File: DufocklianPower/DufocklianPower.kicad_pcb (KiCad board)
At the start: 0 parts

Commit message: finish pcb
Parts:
- added C1: 100n, Capacitor_SMD:C_0805_2012Metric, F.Cu at (175.1, 88.9)
- added C10: 4.7u, Capacitor_SMD:C_0805_2012Metric, F.Cu at (190.6, 72.9)
- added C11: 10u, Capacitor_SMD:C_0805_2012Metric, F.Cu at (190.6, 76.9)
- added C15: 100n, Capacitor_SMD:C_1210_3225Metric, F.Cu at (138.2, 89.6)
- added C16: 100n, Capacitor_SMD:C_1210_3225Metric, F.Cu at (147.9, 101.4)
- added C17: 100n, Capacitor_SMD:C_1210_3225Metric, F.Cu at (142.9, 89.6)
- added C18: 100n, Capacitor_SMD:C_1210_3225Metric, F.Cu at (147.9, 96.7)
- added C19: 100n, Capacitor_SMD:C_0805_2012Metric, F.Cu at (162.8, 80.3)
- added C2: 1u, Capacitor_SMD:C_0805_2012Metric, F.Cu at (146.6, 57.7)
- added C20: 1u, Capacitor_SMD:C_0805_2012Metric, F.Cu at (160.7, 80.3)
- added C21: 22u, Capacitor_SMD:C_1210_3225Metric, F.Cu at (176.8, 99.9)
- added C22: 22u, Capacitor_SMD:C_1210_3225Metric, F.Cu at (173.6, 95.3)
- added C23: 22u, Capacitor_SMD:C_1210_3225Metric, F.Cu at (176.8, 95.3)
- added C24: 22u, Capacitor_SMD:C_1210_3225Metric, F.Cu at (173.6, 99.9)
- added C25: 100n, Capacitor_SMD:C_0805_2012Metric, F.Cu at (166.2, 91.8)
- added C26: 1u, Capacitor_SMD:C_0805_2012Metric, F.Cu at (153.4, 78.8)
- added C27: 47u, Capacitor_SMD:C_0805_2012Metric, F.Cu at (158.3, 72.3)
- added C3: 1u, Capacitor_SMD:C_0805_2012Metric, F.Cu at (146.6, 51.3)
- added C36: 100p, Capacitor_SMD:C_0805_2012Metric, F.Cu at (175.1, 85.4)
- added C37: 100n, Capacitor_SMD:C_0805_2012Metric, F.Cu at (151.1, 57.3)
- added C38: 100n, Capacitor_SMD:C_0805_2012Metric, F.Cu at (183.2, 69.8)
- added C4: 1u, Capacitor_SMD:C_0805_2012Metric, F.Cu at (193.8, 104.1)
- added C40: 100n, Capacitor_SMD:C_0805_2012Metric, F.Cu at (193.8, 100.7)
- added C42: 100p, Capacitor_SMD:C_0805_2012Metric, F.Cu at (182.7, 78.5)
- added C43: 1n, Capacitor_SMD:C_0805_2012Metric, F.Cu at (184.7, 78.5)
- added C44: 2.2n, Capacitor_SMD:C_0805_2012Metric, F.Cu at (180.9, 75.0)
- added C6: 2.2n, Capacitor_SMD:C_0805_2012Metric, F.Cu at (193.0, 54.1)
- added C7: 56p, Capacitor_SMD:C_0805_2012Metric, F.Cu at (193.0, 56.1)
- added C8: 2.2n, Capacitor_SMD:C_0805_2012Metric, F.Cu at (188.4, 53.0)
- added C9: 1u, Capacitor_SMD:C_0805_2012Metric, F.Cu at (190.6, 74.9)
- added J1: 8174, Library:KEYSTONE_8174, F.Cu at (140.5, 99.0)
- added J2: SCREEN, Connector_PinHeader_2.54mm:PinHeader_1x04_P2.54mm_Vertical, F.Cu at (213.5, 101.8)
- added J3: 8174, Library:KEYSTONE_8174, F.Cu at (140.5, 80.0)
- added J4: USB_C_Receptacle_USB2.0_14P, Connector_USB:USB_C_Receptacle_GCT_USB4105-xx-A_16P_TopMnt_Horizontal, F.Cu at (139.2, 65.2)
- added J5: OUT, Connector_AMASS:AMASS_XT60PW-M_1x02_P7.20mm_Horizontal, F.Cu at (190.8, 110.9)
- added L1: 15uH, Library:IND_SER2915H-223KL, F.Cu at (159.6, 115.1)
- added L2: 68uH, Library:IND_BOURNS_SRR1260, F.Cu at (202.4, 59.5)
- added Q1: NMOS, Library:TRANS_BSC027N10NS5ATMA1, F.Cu at (161.3, 94.7)
- added Q2: NMOS, Library:TRANS_BSC027N10NS5ATMA1, F.Cu at (160.7, 88.1)
- added Q4: 2N7002, Package_TO_SOT_SMD:SOT-23, F.Cu at (179.0, 89.8)
- added R1: 87k, Resistor_SMD:R_0603_1608Metric, F.Cu at (169.2, 80.5)
- added R10: 14k7, Resistor_SMD:R_0603_1608Metric, F.Cu at (166.1, 80.5)
- added R11: 400k, Resistor_SMD:R_0603_1608Metric, F.Cu at (194.9, 80.1)
- added R12: 100k, Resistor_SMD:R_0603_1608Metric, F.Cu at (158.9, 80.3)
- added R13: 100k, Resistor_SMD:R_0603_1608Metric, F.Cu at (170.7, 80.5)
- added R14: 100k, Resistor_SMD:R_0603_1608Metric, F.Cu at (196.4, 80.1)
- added R16: 1k, Resistor_SMD:R_0603_1608Metric, F.Cu at (180.9, 78.3)
- added R17: 10k, Resistor_SMD:R_0603_1608Metric, F.Cu at (151.0, 53.9)
- added R19: 10k, Resistor_SMD:R_0603_1608Metric, F.Cu at (183.4, 76.0)
- added R2: 10.7k, Resistor_SMD:R_0603_1608Metric, F.Cu at (175.1, 87.2)
- added R20: 4.7k, Resistor_SMD:R_0603_1608Metric, F.Cu at (175.1, 90.7)
- added R21: 120k, Resistor_SMD:R_0603_1608Metric, F.Cu at (154.0, 73.1)
- added R22: 5m, Resistor_SMD:R_0603_1608Metric, F.Cu at (158.3, 75.5)
- added R23: 2m, Library:FC4L90_OHM, F.Cu at (184.8, 95.3)
- added R24: 1k, Resistor_SMD:R_0603_1608Metric, F.Cu at (179.0, 85.5)
- added R25: 10k, Resistor_SMD:R_0603_1608Metric, F.Cu at (181.5, 69.8)
- added R26: 2.7k, Resistor_SMD:R_0603_1608Metric, F.Cu at (155.6, 60.2)
- added R27: 2.7k, Resistor_SMD:R_0603_1608Metric, F.Cu at (155.6, 61.7)
- added R28: 2m, Library:FC4L90_OHM, F.Cu at (185.5, 104.2)
- added R29: 2.7k, Resistor_SMD:R_0603_1608Metric, F.Cu at (211.5, 67.9)
- added R3: 100k, Resistor_SMD:R_0603_1608Metric, F.Cu at (190.8, 62.9)
- added R30: 5.1k, Resistor_SMD:R_0603_1608Metric, F.Cu at (146.1, 67.0)
- added R31: 5.1k, Resistor_SMD:R_0603_1608Metric, F.Cu at (146.6, 63.0)
- added R32: 100k, Resistor_SMD:R_0603_1608Metric, F.Cu at (179.0, 87.1)
- added R33: 100, Resistor_SMD:R_0603_1608Metric, F.Cu at (194.0, 105.9)
- added R34: 100, Resistor_SMD:R_0603_1608Metric, F.Cu at (193.8, 102.4)
- added R35: 2.7k, Resistor_SMD:R_0603_1608Metric, F.Cu at (206.4, 122.5)
- added R4: 316k, Resistor_SMD:R_0603_1608Metric, F.Cu at (193.0, 57.9)
- added R5: 101k, Resistor_SMD:R_0603_1608Metric, F.Cu at (193.0, 59.3)
- added R6: 470k, Resistor_SMD:R_0603_1608Metric, F.Cu at (193.0, 52.4)
- added R7: 5m, Resistor_SMD:R_2512_6332Metric, F.Cu at (154.3, 93.5)
- added R8: 615k, Resistor_SMD:R_0603_1608Metric, F.Cu at (164.6, 80.5)
- added R9: 10k, Resistor_SMD:R_0603_1608Metric, F.Cu at (167.6, 80.5)
- added SW1: RST, Button_Switch_SMD:SW_Push_1P1T-SH_NO_CK_KMR2xxG, F.Cu at (154.2, 55.0)
- added SW2: BOOT, Button_Switch_SMD:SW_Push_1P1T-SH_NO_CK_KMR2xxG, F.Cu at (178.9, 68.7)
- added SW3: Voltage Control, Rotary_Encoder:RotaryEncoder_Alps_EC11E-Switch_Vertical_H20mm, F.Cu at (205.7, 84.8)
- added SW4: Current Control, Rotary_Encoder:RotaryEncoder_Alps_EC11E-Switch_Vertical_H20mm, F.Cu at (210.6, 105.5)
- added U1: ~, Library:VQFN24_RGY_TEX, F.Cu at (168.3, 86.7)
- added U11: INA228, Package_SO:TSSOP-10_3x3mm_P0.5mm, F.Cu at (193.6, 95.6)
- added U2: LM5164DDA, Package_SO:HSOP-8-1EP_3.9x4.9mm_P1.27mm_EP2.41x3.1mm_ThermalVias, F.Cu at (186.7, 60.5)
- added U3: ADS8681RUM, Package_DFN_QFN:QFN-16-1EP_4x4mm_P0.65mm_EP2.7x2.7mm, F.Cu at (196.6, 74.6)
- added U4: DAC8562, Package_SO:TSSOP-10_3x3mm_P0.5mm, F.Cu at (165.0, 76.3)
- added U5: INA241A4xD, Package_SO:SOIC-8_3.9x4.9mm_P1.27mm, F.Cu at (184.9, 85.6)
- added U6: ESP32-S3-WROOM-1, RF_Module:ESP32-S3-WROOM-1, F.Cu at (167.2, 54.1)
- added U7: OPA188xxD, Package_SO:SOIC-8_3.9x4.9mm_P1.27mm, F.Cu at (176.2, 78.4)
- added U8: AP2112K-3.3, Package_TO_SOT_SMD:SOT-23-5, F.Cu at (146.6, 54.5)
- added U9: REF6025xDGK, Package_SO:VSSOP-8_3x3mm_P0.65mm, F.Cu at (153.5, 75.9)
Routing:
- net +3V3: track 0.00 -> 217.1 mm, vias 0 -> 8
- net VBUS: track 0.00 -> 83.6 mm, vias 0 -> 59
- net /C_{CF}: track 0.00 -> 79.0 mm
- net /SCL: track 0.00 -> 76.4 mm, vias 0 -> 2
- net /SDA: track 0.00 -> 75.7 mm, vias 0 -> 2
- net /CEN_{B}: track 0.00 -> 72.2 mm
- net /CEN_{A}: track 0.00 -> 70.0 mm
- net /VOUT_{0}: track 0.00 -> 56.0 mm, vias 0 -> 46
- net /~{RST}: track 0.00 -> 55.1 mm
- net +5V: track 0.00 -> 53.4 mm, vias 0 -> 5
- net /SDI: track 0.00 -> 52.0 mm
- net /VEN_{B}: track 0.00 -> 50.3 mm
- net /~{ALRT}: track 0.00 -> 49.9 mm, vias 0 -> 2
- net /VEN_{A}: track 0.00 -> 46.5 mm
- net /~{CS}: track 0.00 -> 42.4 mm
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- added copper zone on In2.Cu, net +5V
- added copper zone on F.Cu, net /ISNS+
- added copper zone on F.Cu, net /SW
- added copper zone on F.Cu, net /VOUT
- added copper zone on F.Cu, net /VOUT_{0}
- added copper zone on In2.Cu, net /VOUT_{0}
- added copper zone on F.Cu, net /VOUT_{1}
- added copper zone on B.Cu, net GNDREF
- added copper zone on F.Cu, net GNDREF
- added copper zone on In1.Cu, net GNDREF
- added copper zone on F.Cu, net VBUS
- added copper zone on In2.Cu, net VBUS
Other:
- board outline added: 80 x 80 mm
- copper layers 0 -> 4
- board text added: "{ "ViaStitcher": "0.3.4", "stitch_zone_0": { "HSpacing": "1", "VSpacing": "1", "HOffset": "0", "VOffset": "0", "Clearance": "0", "FillStyle": "Standard", "OnlyFilledCopper": true } }"
- board text added: "{ "ViaStitcher": "0.3.4", "stitch_zone_0": { "HSpacing": "5", "VSpacing": "5", "HOffset": "0", "VOffset": "0", "Clearance": "0", "FillStyle": "Stagger", "OnlyFilledCopper": true } }"

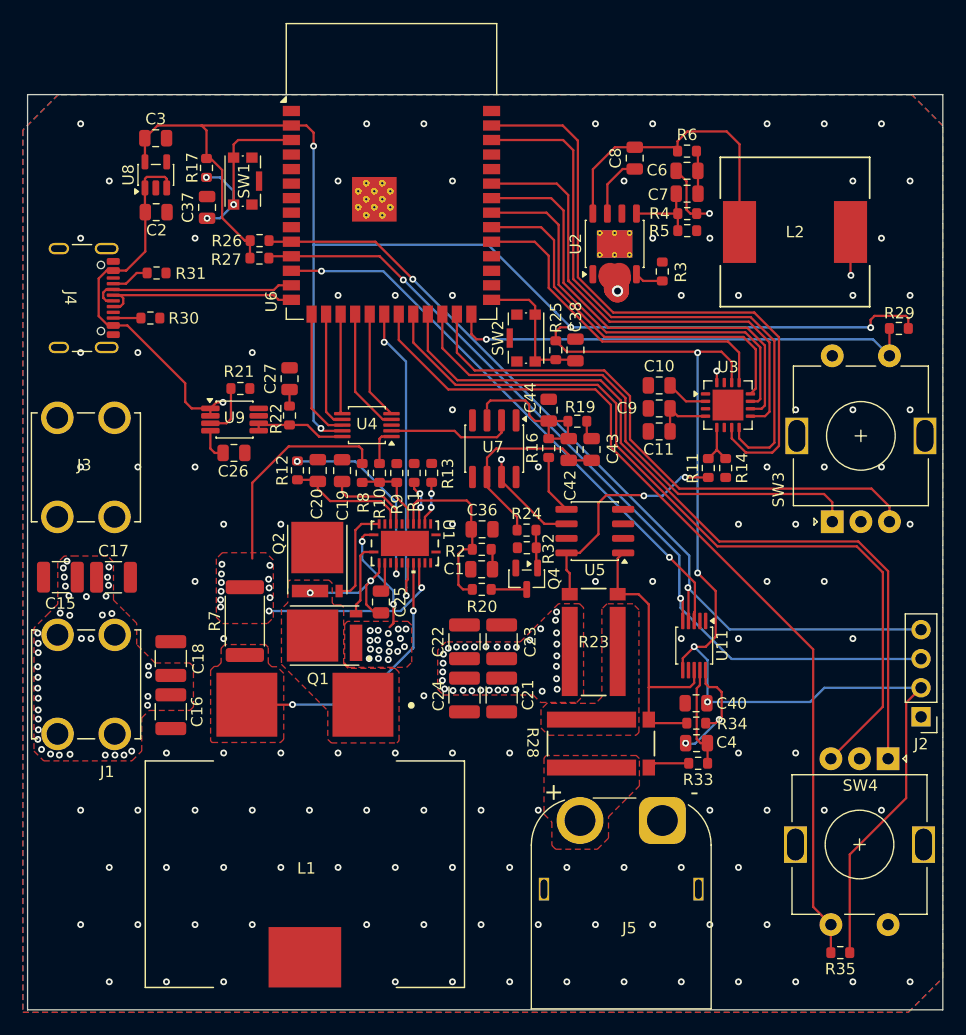
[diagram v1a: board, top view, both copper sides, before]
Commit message: finish via + change ind
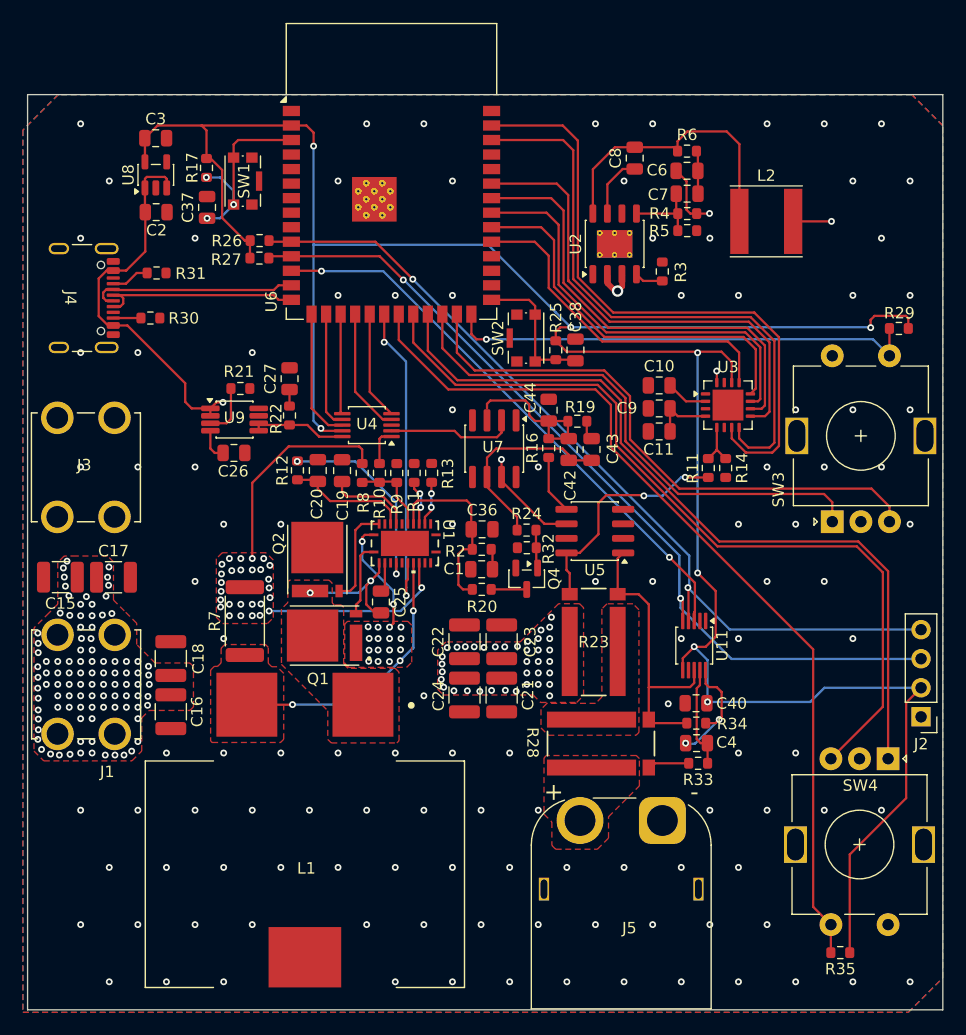
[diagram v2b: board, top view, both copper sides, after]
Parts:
- L2: footprint Library:IND_BOURNS_SRR1260 -> Inductor_SMD:L_Taiyo-Yuden_NR-60xx
- moved L2 2.68 mm to (199.9, 58.5)
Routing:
- net VBUS: track 83.6 -> 83.1 mm, vias 59 -> 117
- net GNDREF: vias 115 -> 116
- net /VOUT_{0}: vias 46 -> 68
- net /ISNS+: vias 2 -> 3

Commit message: less drc
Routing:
- net GNDREF: vias 116 -> 118
- net /ISNS+: vias 3 -> 2
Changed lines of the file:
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@@
 	)
 	(via
+		(at 179.61 62.63)
+		(size 0.6)
+		(drill 0.3)
+		(layers "F.Cu" "B.Cu")
+		(free yes)
+		(net "GNDREF")
+	)
+	(via
 		(at 172.5 105)
 		(size 0.6)
@@
 	)
 	(via
+		(at 176.49 67.69)
+		(size 0.6)
+		(drill 0.3)
+		(layers "F.Cu" "B.Cu")
+		(free yes)
+		(net "GNDREF")
+	)
+	(via
 		(at 210 80)
 		(size 0.6)
@@
 	)
 	(via
-		(at 167.925 96.935)
-		(size 0.6)
-		(drill 0.3)
-		(layers "F.Cu" "B.Cu")
-		(net "/ISNS+")
-	)
-	(via
 		(at 158.52 100.77)
 		(size 0.6)
@@
 			(smoothing fillet)
 			(radius 0.2)
-			(island_removal_mode 1)
+			(island_removal_mode 2)
+			(island_area_min 25)
 		)
 		(polygon

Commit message: bom.csv
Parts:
- removed C21, C23, C24: 22u, Capacitor_SMD:C_1210_3225Metric
- removed J5: OUT, Connector_AMASS:AMASS_XT60PW-M_1x02_P7.20mm_Horizontal
- removed U7: OPA188xxD, Package_SO:SOIC-8_3.9x4.9mm_P1.27mm
- added J6: Vout, Connector:Banana_Cliff_FCR7350Y_S16N-PC_Horizontal, F.Cu at (180.5, 113.8)
- added J7: Screw_Terminal_01x01, Connector:Banana_Cliff_FCR7350Y_S16N-PC_Horizontal, F.Cu at (194.3, 113.6)
- added U10: TLV3501AID, Package_SO:SOIC-8_3.9x4.9mm_P1.27mm, F.Cu at (176.2, 78.4)
- C22: footprint Capacitor_SMD:C_1210_3225Metric -> Capacitor_SMD:C_Elec_10x10.2
- R11: footprint Resistor_SMD:R_0603_1608Metric -> Resistor_SMD:R_0805_2012Metric
- moved C22 4.92 mm to (175.5, 99.8), turned to -90 degrees
- moved R23 0.82 mm to (185.7, 95.2)
- moved R28 0.79 mm to (186.3, 104.2)
- moved R11 0.29 mm to (194.6, 79.9)
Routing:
- net /VOUT: track 3.68 -> 2.85 mm
- net /SW: track 11.4 -> 10.6 mm
- net /VOUT_{0}: vias 68 -> 106
